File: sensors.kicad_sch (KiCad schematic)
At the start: 43 parts, among them J3 SM04B-SRSS-TB(LF)(SN), J5 Micro_SD_Card, U10 SHT45-AD1B-R2, U11 RFM95W-915S2, U12 W25Q128JVSIQ, U16 PCA9685BS, U5 SAM-M10Q-00B, U6 MS860702BA01-50, U7 DPS310, U8 H3LIS331DL, U9 LSM6DSO32TR

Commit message: Organized Schematics & Fixed Notes
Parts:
- removed J3: SM04B-SRSS-TB(LF)(SN), JST_SM04B-SRSS-TB(LF)(SN), symbol SM04B-SRSS-TB_LF__SN_:SM04B-SRSS-TB(LF)(SN)
- added J12: RF Antenna, TE_5449692-1, symbol 5449692-1:5449692-1
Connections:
- net GND: now also J12.GND; no longer R32.1, U16.26 (A0)
- net RFM95W_ANT: now also J12.1
- net at U9.10 (NC): now also U9.11 (NC)
- net at U16.12 (LED8): now also U16.13 (LED9), U16.14 (LED10), U16.15 (LED11), U16.16 (LED12), U16.17 (LED13), U16.18 (LED14), U16.19 (LED15)
- new net: R32.1, U16.26 (A0)
- no-connect marks 11 -> 3
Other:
- note added: "I2C Address - 0x41"
- note added: "I2C Address - 0x42"
- note added: "I2C Address - 0x44"
- note added: "I2C Address - Humidity: 0x40, Pressure: 0x76"
- note added: "Verify Footprint"
- note added: "W25Q128 (FLASH) - SPI (QSPI?)"
- note removed: "0x40, 0x76"
- note removed: "0x41"
- note removed: "0x42"
- note removed: "0x44"
- note removed: "RFD900 - UART (ESP32)"
- note removed: "W25Q128 (FLASH) - SPI (QSPI)"
- company: (none) -> nyuad.space
- title: (none) -> Sensors & Active Components
- moved on the sheet: BT1, C11, C12, C13, C14, C15, C16, C17, C18, C19, C20, C21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

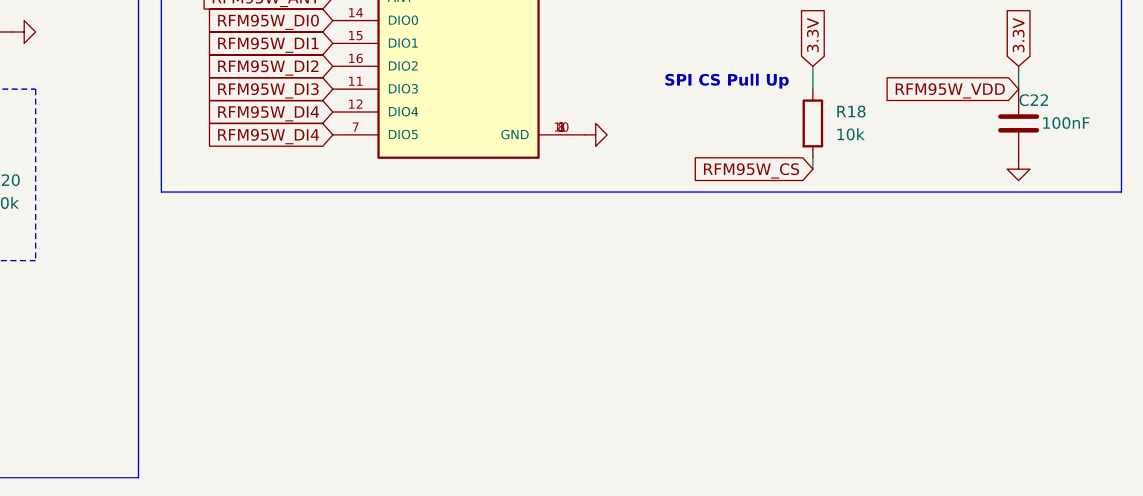
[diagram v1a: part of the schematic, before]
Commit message: Added OSH Logo
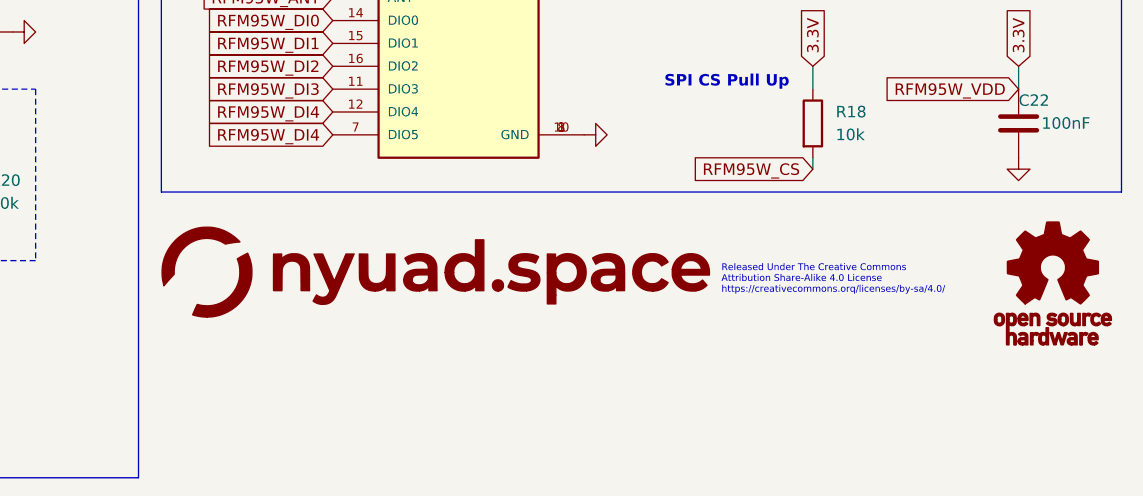
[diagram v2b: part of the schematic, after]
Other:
- note added: "Released Under The Creative Commons Attribution Share-Alike 4.0 License https://creativecommons.orq/licenses/by-sa/4.0/"
- company: nyuad.space -> Aether Flight Computer
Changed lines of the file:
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@@
   (title_block
     (title "Sensors & Active Components")
-    (company "nyuad.space")
-    (comment 1 "Aether Flight Computer")
+    (company "Aether Flight Computer")
   )
   (junction (at 46.99 166.37) (diameter 0) (color 0 0 0 0)
@@
   (text "SPI CS Pull Up" (at 233.68 152.4 0)
     (effects (font (size 1.27 1.27) bold) (justify left bottom))
+  )
+  (text "Released Under The Creative Commons\nAttribution Share-Alike 4.0 License\nhttps://creativecommons.orq/licenses/by-sa/4.0/"
+    (at 240.03 175.26 0)
+    (effects (font (face "KiCad Font") (size 0.75 0.75)) (justify left bottom))
   )
   (text "SPI CS Pull Up" (at 142.24 193.04 0)
@@
         (path "/e12346fa-509d-4de9-8ab1-dced307292db/b5ec7ecd-943d-4169-981a-c46b6432f873"
           (reference "#PWR015") (unit 1)
+        )
+      )
+    )
+  )
+  (symbol (lib_id "nyuad_space:LOGO") (at 208.28 172.72 0) (unit 1)
+    (in_bom yes) (on_board yes) (dnp no) (fields_autoplaced)
+    (property "Reference" "#G2" (at 208.28 168.3609 0)
+      (effects (font (size 1.27 1.27)) hide)
+    )
+    (property "Value" "LOGO" (at 208.28 177.0791 0)
+      (effects (font (size 1.27 1.27)) hide)
+    )
+    (property "Footprint" "" (at 208.28 172.72 0)
+      (effects (font (size 1.27 1.27)) hide)
+    )
+    (property "Datasheet" "" (at 208.28 172.72 0)
+      (effects (font (size 1.27 1.27)) hide)
+    )
+    (instances
+      (project "aether"
+        (path "/e12346fa-509d-4de9-8ab1-dced307292db"
+          (reference "#G2") (unit 1)
+        )
+        (path "/e12346fa-509d-4de9-8ab1-dced307292db/b5ec7ecd-943d-4169-981a-c46b6432f873"
+          (reference "#G5") (unit 1)
         )
       )
@@
         )
       )
+    )
+  )
+  (symbol (lib_id "osh_logo:LOGO") (at 276.86 173.99 0) (unit 1)
+    (in_bom yes) (on_board yes) (dnp no) (fields_autoplaced)
+    (property "Reference" "#G1" (at 276.86 167.7874 0)
+      (effects (font (size 1.27 1.27)) hide)
+    )
+    (property "Value" "LOGO" (at 276.86 180.1926 0)
+      (effects (font (size 1.27 1.27)) hide)
+    )
+    (property "Footprint" "" (at 276.86 173.99 0)
+      (effects (font (size 1.27 1.27)) hide)
+    )
+    (property "Datasheet" "" (at 276.86 173.99 0)
+      (effects (font (size 1.27 1.27)) hide)
+    )
+    (instances
+      (project "aether"
+        (path "/e12346fa-509d-4de9-8ab1-dced307292db"
+          (reference "#G1") (unit 1)
+        )
+        (path "/e12346fa-509d-4de9-8ab1-dced307292db/b5ec7ecd-943d-4169-981a-c46b6432f873"
+          (reference "#G6") (unit 1)
+        )
+      )

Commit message: Updated files
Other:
- note removed: "Released Under The Creative Commons Attribution Share-Alike 4.0 License https://creativecommons.orq/licenses/by-sa/4.0/"
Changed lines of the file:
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@@
     (effects (font (size 1.27 1.27) bold) (justify left bottom))
-  )
-  (text "Released Under The Creative Commons\nAttribution Share-Alike 4.0 License\nhttps://creativecommons.orq/licenses/by-sa/4.0/"
-    (at 240.03 175.26 0)
-    (effects (font (face "KiCad Font") (size 0.75 0.75)) (justify left bottom))
   )
   (text "SPI CS Pull Up" (at 142.24 193.04 0)

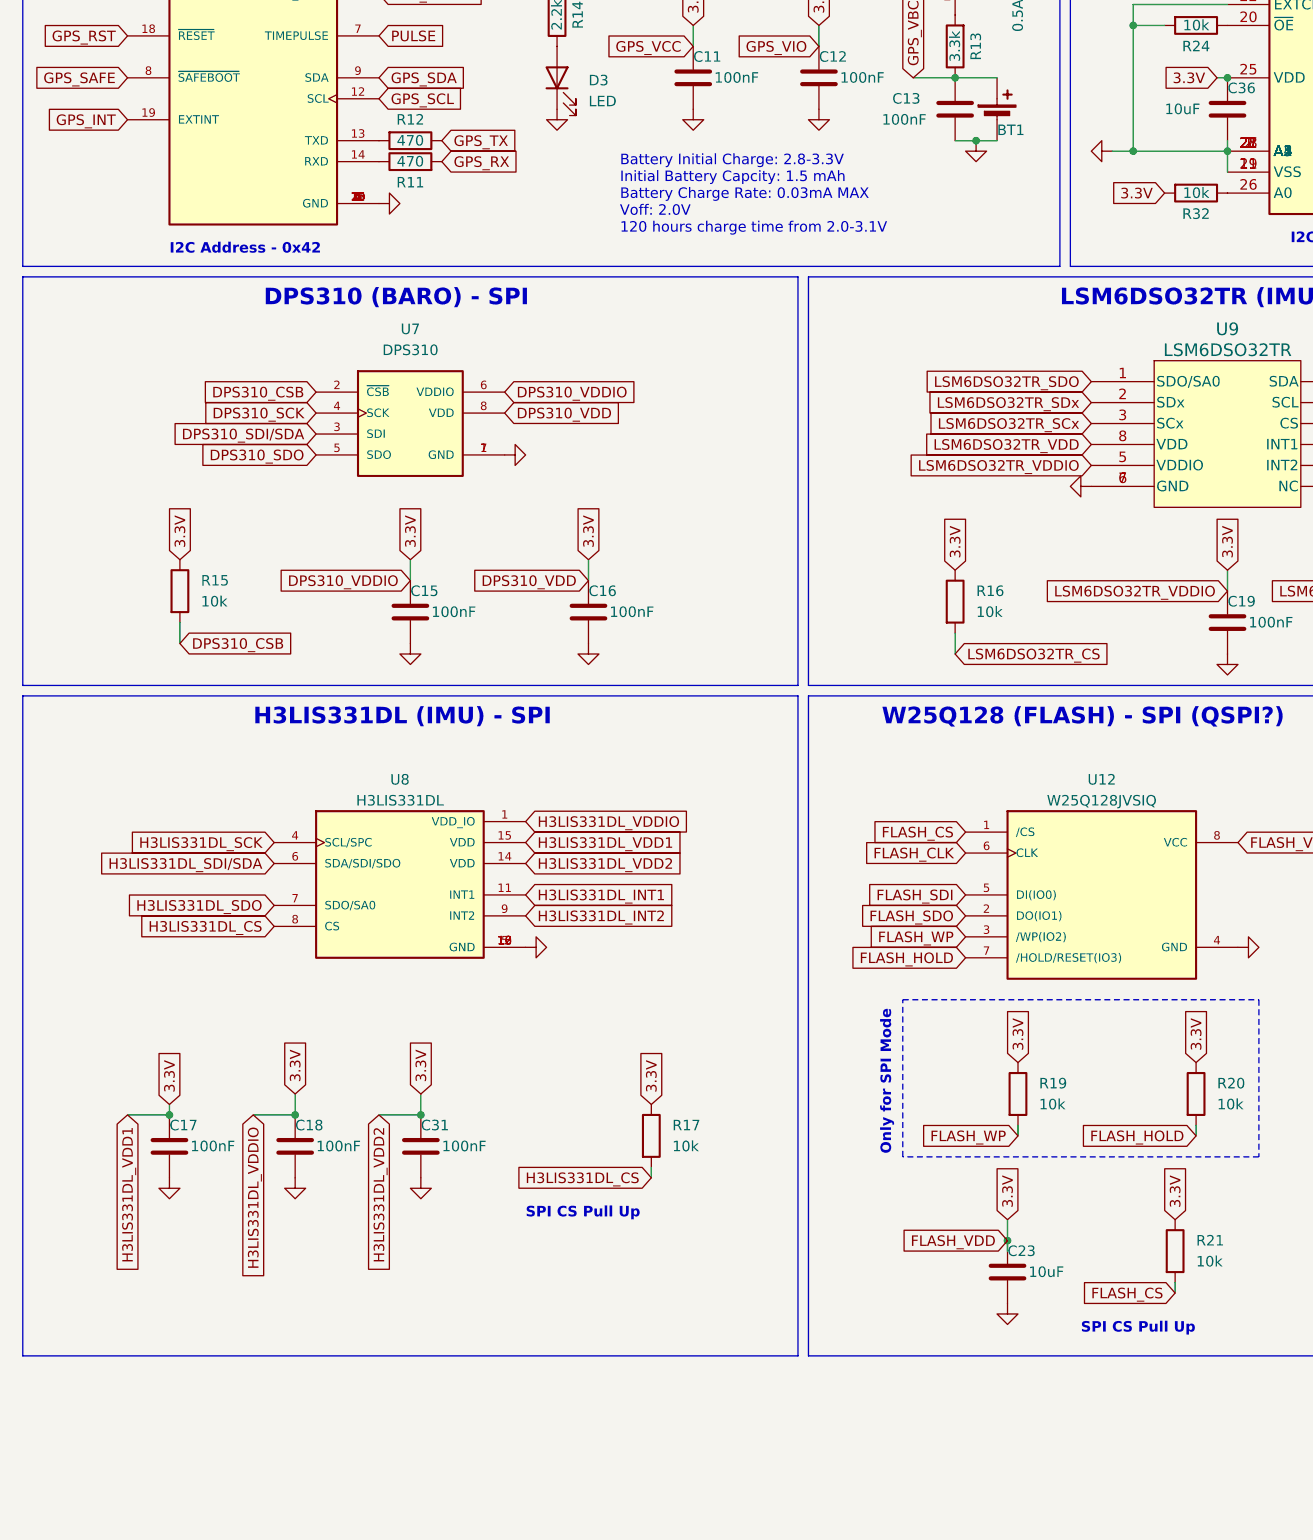
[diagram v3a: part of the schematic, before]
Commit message: Added INA219
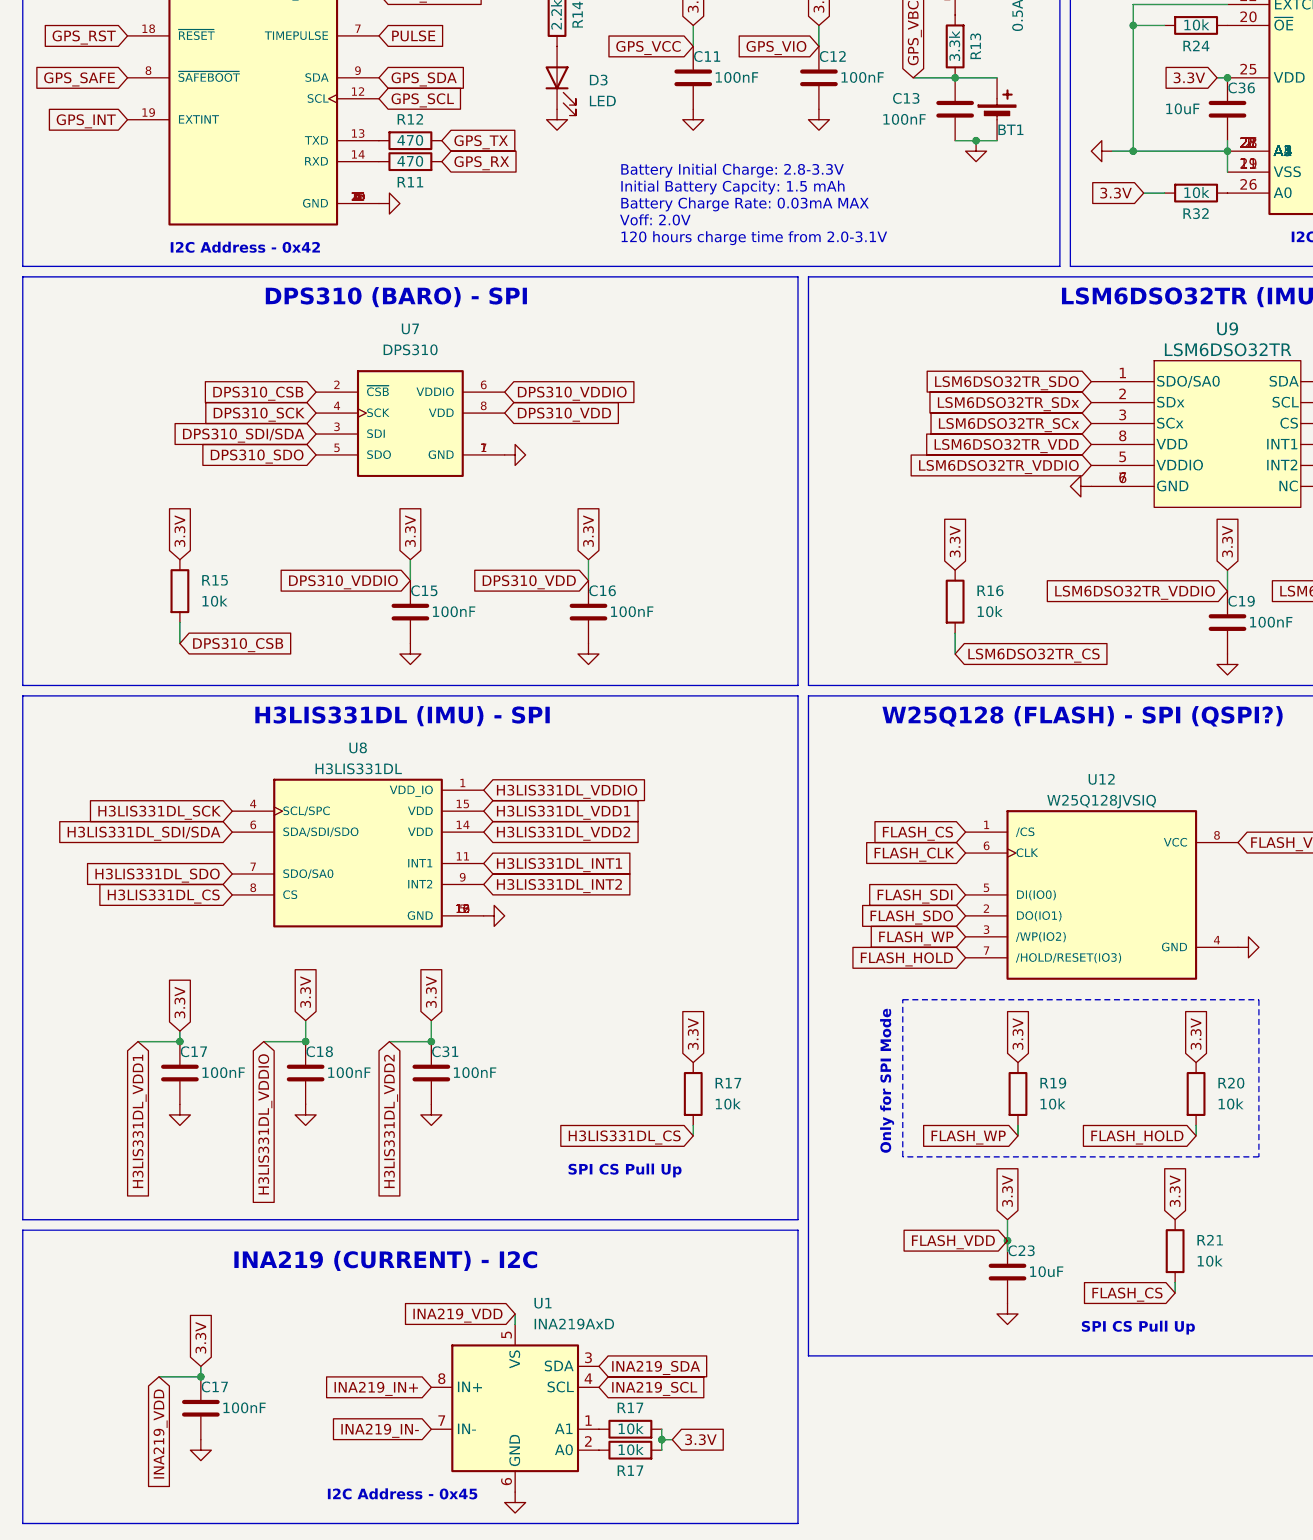
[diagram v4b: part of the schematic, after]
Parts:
- added C17: 100nF, Capacitor_SMD:C_0201_0603Metric, symbol Device:C
- added R17 (x2): 10k, Resistor_SMD:R_0201_0603Metric, symbol Device:R
- added U1: INA219AxD, Package_SO:SOIC-8_3.9x4.9mm_P1.27mm, symbol Sensor_Energy:INA219AxD
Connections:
- net 3.3V: now also C17.1, R17.2, R17.2, U1.5 (VS)
- net GND: now also C17.2, U1.6 (GND)
- new net: R17.1, U1.1 (A1)
- new net: R17.1, U1.2 (A0)
- new net INA219_IN+: U1.8 (IN+)
- new net INA219_IN-: U1.7 (IN-)
- new net INA219_SCL: U1.4 (SCL)
- new net INA219_SDA: U1.3 (SDA)
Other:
- note added: "I2C Address - 0x45"
- note added: "INA219 (CURRENT) - I2C"
- moved on the sheet: C17, C18, C31, R17, U8

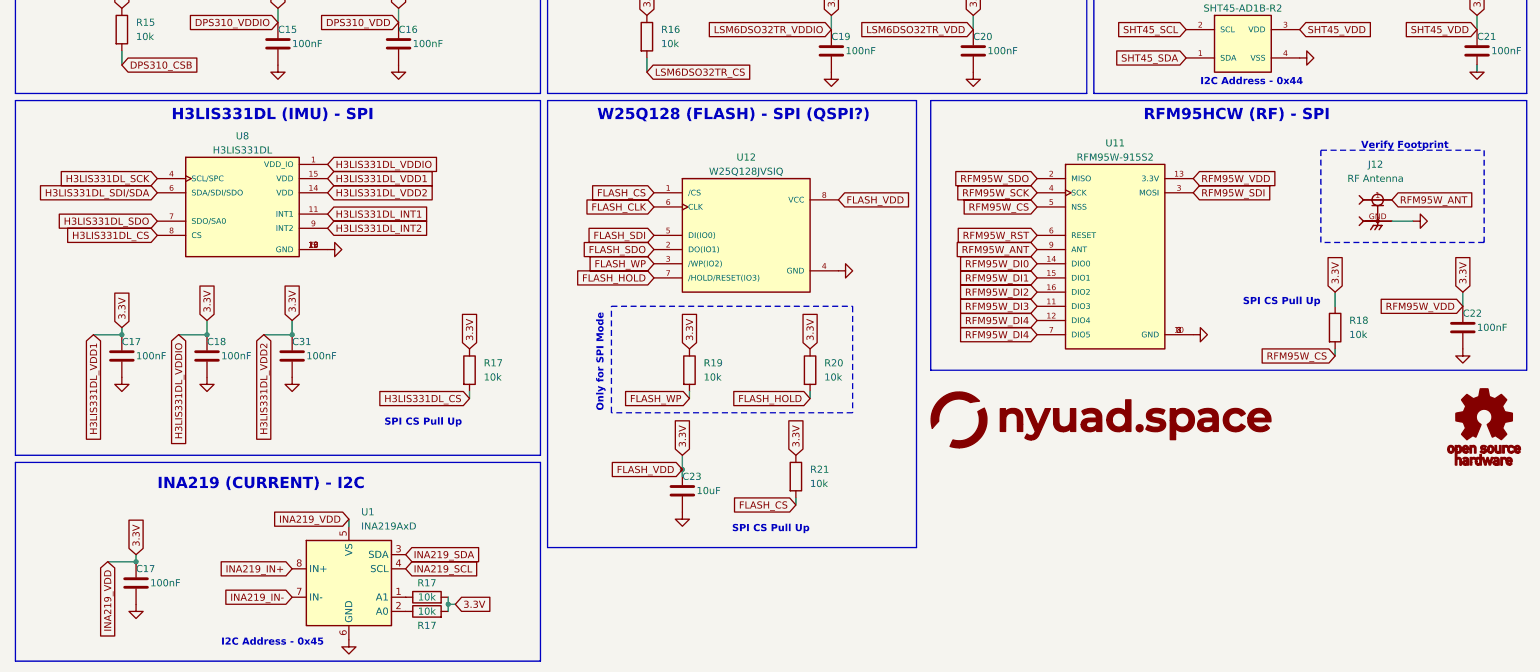
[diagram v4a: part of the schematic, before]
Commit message: Added connectors
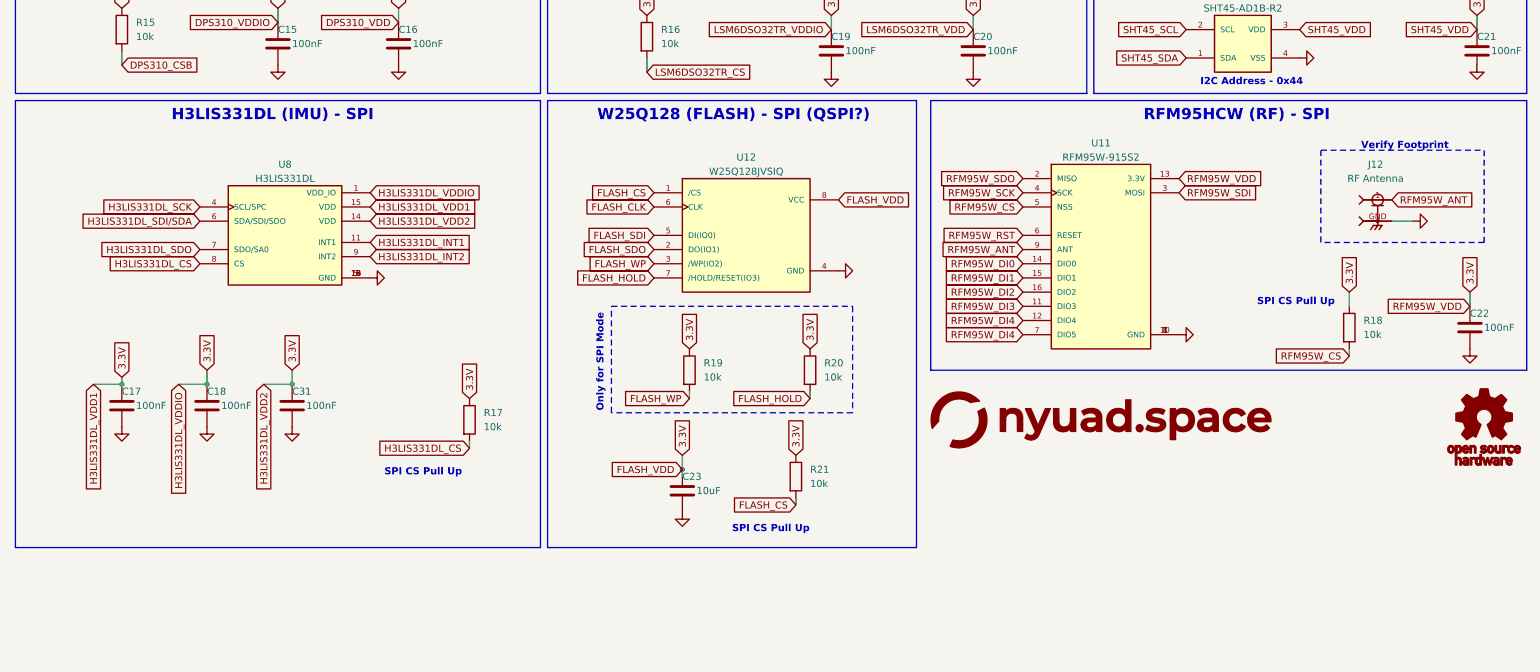
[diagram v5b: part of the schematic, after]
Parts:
- removed C17: 100nF, Capacitor_SMD:C_0201_0603Metric, symbol Device:C
- removed R17 (x2): 10k, Resistor_SMD:R_0201_0603Metric, symbol Device:R
- removed U1: INA219AxD, Package_SO:SOIC-8_3.9x4.9mm_P1.27mm, symbol Sensor_Energy:INA219AxD
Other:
- note removed: "I2C Address - 0x45"
- note removed: "INA219 (CURRENT) - I2C"
- moved on the sheet: C17, C18, C22, C31, R17, R18, U11, U8
